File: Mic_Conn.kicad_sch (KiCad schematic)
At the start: 16 parts, among them J1 JST_SUR_1x5_BM05B-SURS-TB-LF-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, J2 JST_SUR_1x5_BM05B-SURS-TB-LF-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, U1 TPD4E05U06QDQARQ1, U6 TPD4E05U06QDQARQ1

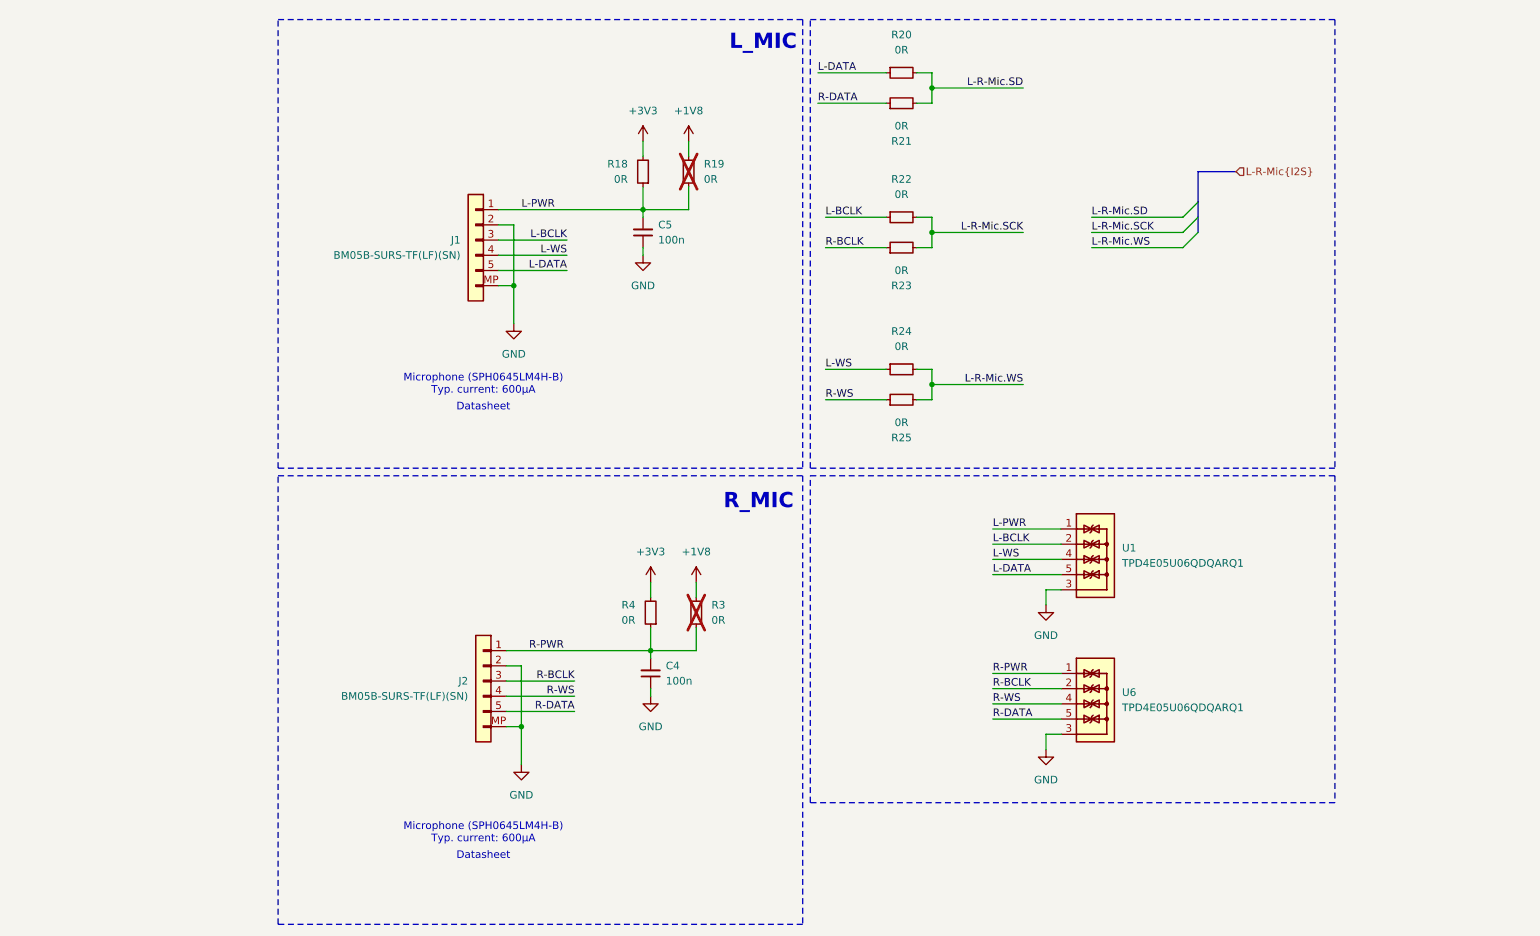
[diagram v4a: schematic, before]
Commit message: [#71555] Add debug I2S conn
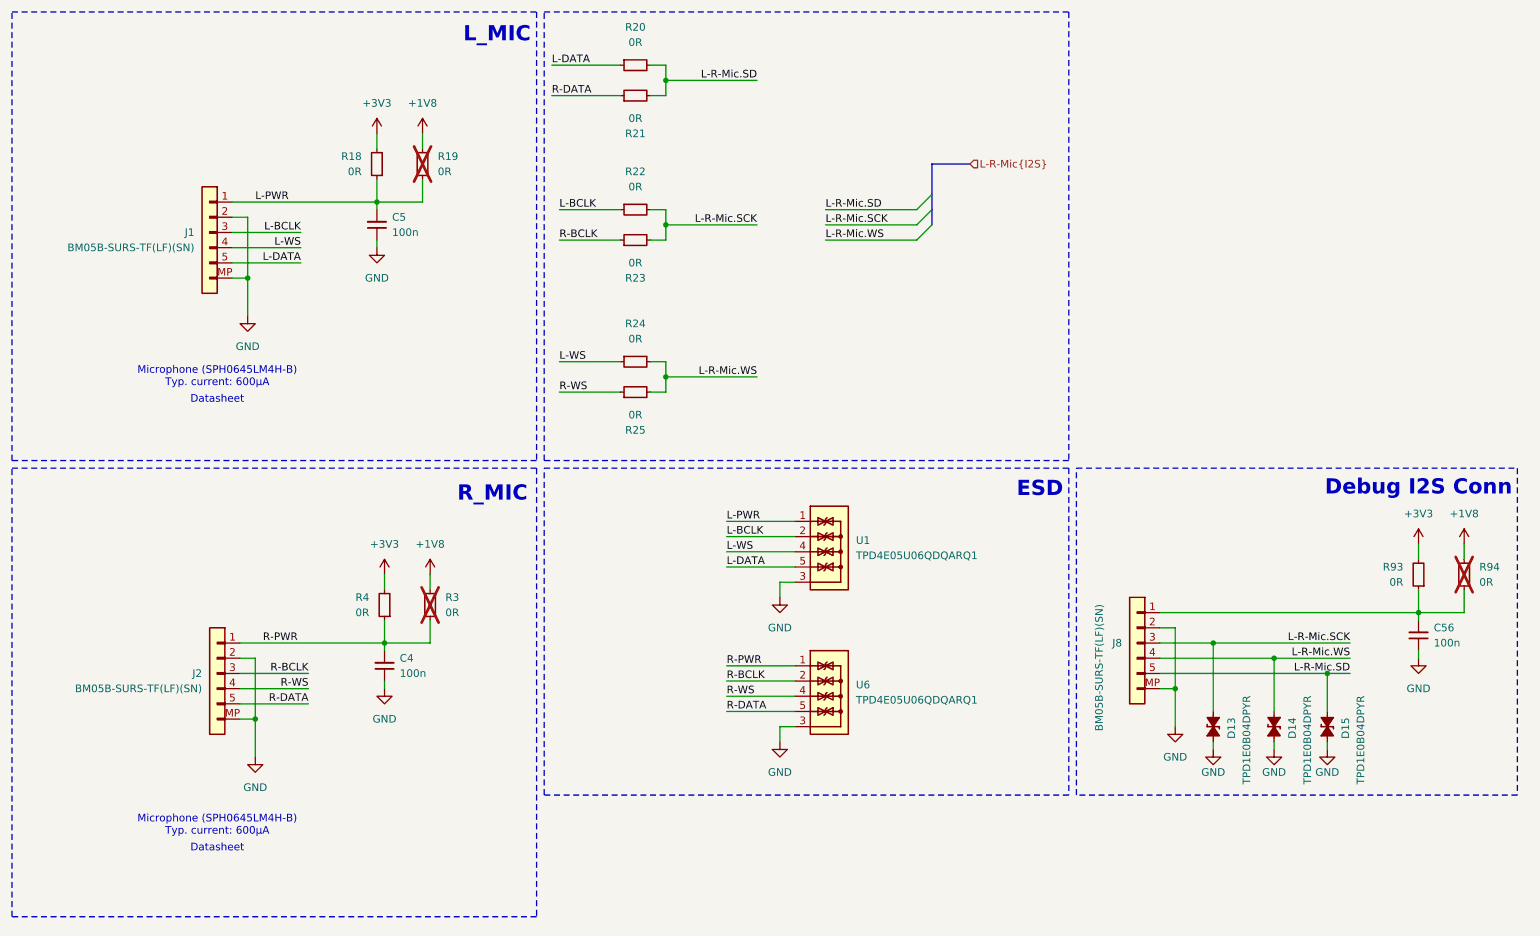
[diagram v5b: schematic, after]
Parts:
- added C56: C_100n_0402, antmicro-footprints:C_0402_1005Metric, symbol antmicroCapacitors0402:C_100n_0402
- added D13, D14, D15: TPD1E0B04_XDFN-2, antmicro-footprints:XDFN-2_1x0.60mm, symbol antmicroTVSDiodes:TPD1E0B04_XDFN-2
- added J8: JST_SUR_1x5_BM05B-SURS-TB-LF-SN, antmicro-footprints:Conn_JST_SUR_1x5_BM05B-SURS-TF-LF-SN, symbol antmicroWire2BoardConnectors:JST_SUR_1x5_BM05B-SURS-TB-LF-SN
- added R93, R94: R_0R_0402, antmicro-footprints:R_0402_1005Metric, symbol antmicroResistors0402:R_0R_0402
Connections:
- net +1V8: now also R94.2
- net +3V3: now also R93.2
- net GND: now also C56.1, D13.1 (C), D14.1 (C), D15.1 (C), J8.2, J8.MP
- net L-R-Mic.SCK: now also D13.2 (A), J8.3
- net L-R-Mic.SD: now also D15.2 (A), J8.5
- net L-R-Mic.WS: now also D14.2 (A), J8.4
- new net: C56.2, J8.1, R93.1, R94.1
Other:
- note added: "Debug I2S Conn"
- note added: "ESD"
- moved on the sheet: C4, C5, J1, J2, R18, R19, R20, R21, R22, R23, R24, R25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
